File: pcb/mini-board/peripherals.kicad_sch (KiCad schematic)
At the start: 20 parts, among them J2 Conn_02x14_Odd_Even, J3 SD Card Board, J8 SERIAL, U15 SST39SF040, U16 AS6C4008-55, U19 W65C22NxP, U21 W65C51NxP, U22 MAX232, Y1 1.8432 MHz

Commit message: Pre-fourlayerboard commit
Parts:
- J2: value Conn_02x14_Odd_Even -> EXPANSION BUS; footprint Connector_PinHeader_2.54mm:PinHeader_2x14_P2.54mm_Vertical -> Connector_PinHeader_2.54mm:PinHeader_2x20_P2.54mm_Vertical; symbol Connector_Generic:Conn_02x14_Odd_Even -> Connector_Generic:Conn_02x20_Odd_Even
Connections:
- net CA1: now also J2.24 (Pin_24); no longer J2.20 (Pin_20)
- net CA2: now also J2.26 (Pin_26); no longer J2.22 (Pin_22)
- net CB1: now also J2.23 (Pin_23); no longer J2.19 (Pin_19)
- net CB2: now also J2.25 (Pin_25); no longer J2.21 (Pin_21)
- net CLK: now also J2.30 (Pin_30); no longer J2.26 (Pin_26)
- net GND: now also J2.11 (Pin_11), J2.12 (Pin_12), J2.21 (Pin_21), J2.22 (Pin_22), J2.31 (Pin_31), J2.32 (Pin_32), J2.39 (Pin_39), J2.40 (Pin_40); no longer J2.27 (Pin_27), J2.28 (Pin_28)
- net PA4: now also J2.14 (Pin_14); no longer J2.12 (Pin_12)
- net PA5: now also J2.16 (Pin_16); no longer J2.14 (Pin_14)
- net PA6: now also J2.18 (Pin_18); no longer J2.16 (Pin_16)
- net PA7: now also J2.20 (Pin_20); no longer J2.18 (Pin_18)
- net PB4: now also J2.13 (Pin_13); no longer J2.11 (Pin_11)
- net PB5: now also J2.15 (Pin_15); no longer J2.13 (Pin_13)
- net PB6: now also J2.17 (Pin_17); no longer J2.15 (Pin_15)
- net PB7: now also J2.19 (Pin_19); no longer J2.17 (Pin_17)
- net RxD1: now also J2.36 (Pin_36)
- net R/~{W}: now also J2.27 (Pin_27); no longer J2.23 (Pin_23)
- net TxD1: now also J2.34 (Pin_34)
- net VCC: now also J2.37 (Pin_37), J2.38 (Pin_38)
- net ~{NMI}: now also J2.29 (Pin_29); no longer J2.25 (Pin_25)
- net ~{RES}: now also J2.28 (Pin_28); no longer J2.24 (Pin_24)
- net ~{VIA_CS}: now also J2.33 (Pin_33)
- net ~{IRQ} renamed ~{IRQ22}
- net ~{IRQ22}: now also J2.35 (Pin_35); no longer U21.26 (~{IRQ})
- new net ~{IRQ51}: U21.26 (~{IRQ})
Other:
- moved on the sheet: C24

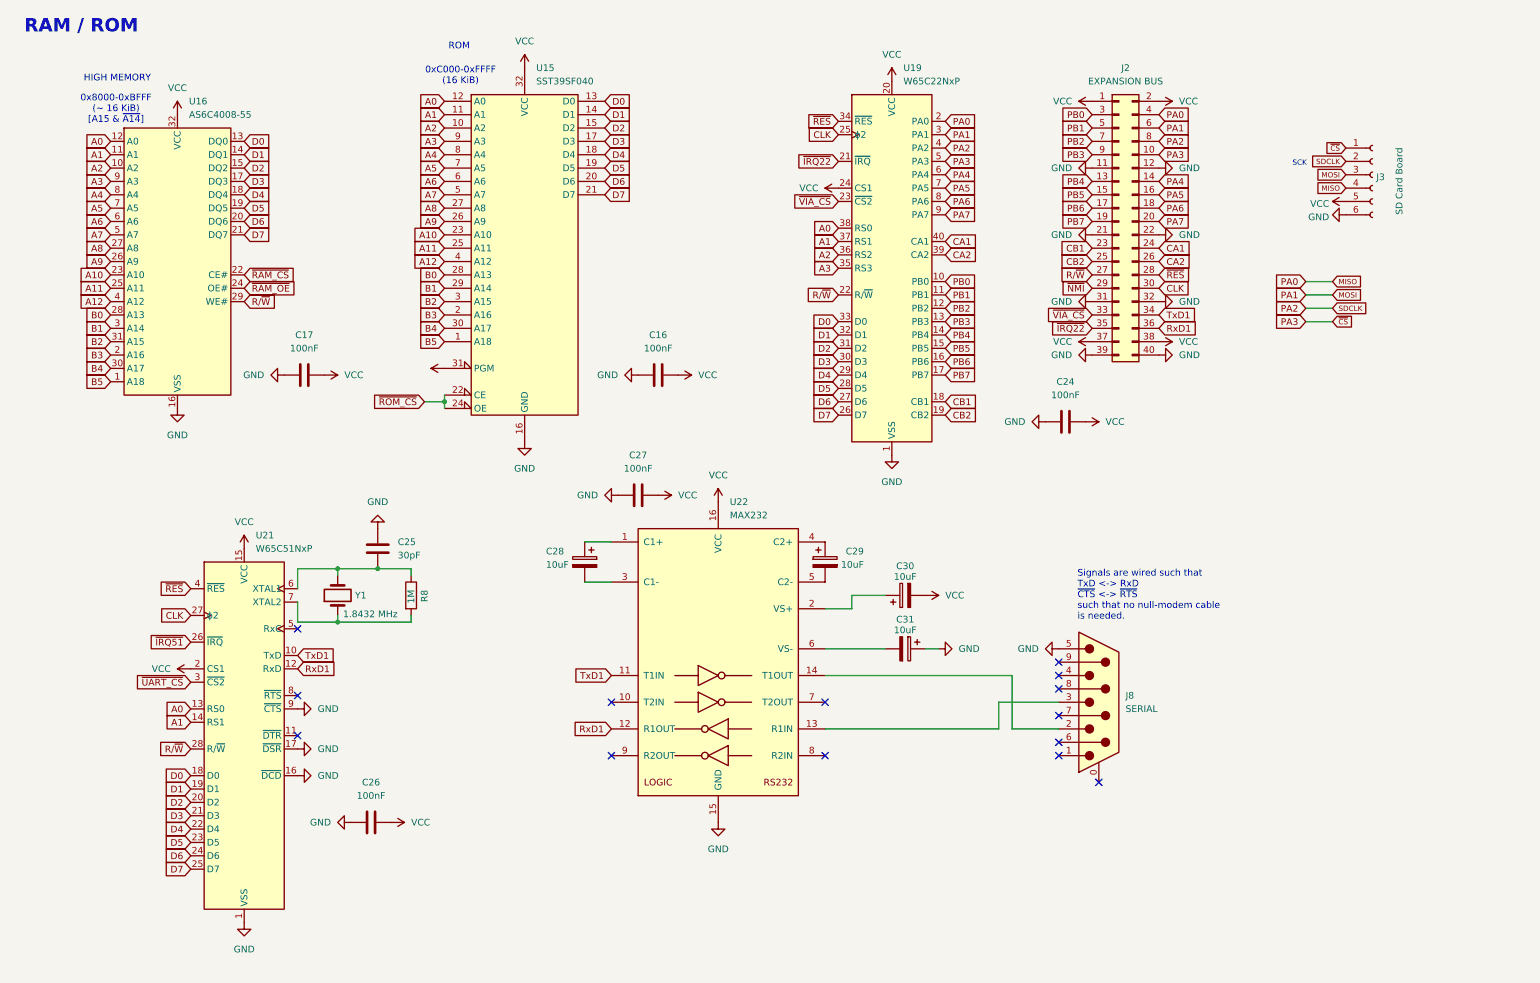
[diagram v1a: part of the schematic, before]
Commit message: Adding documentation to schematics
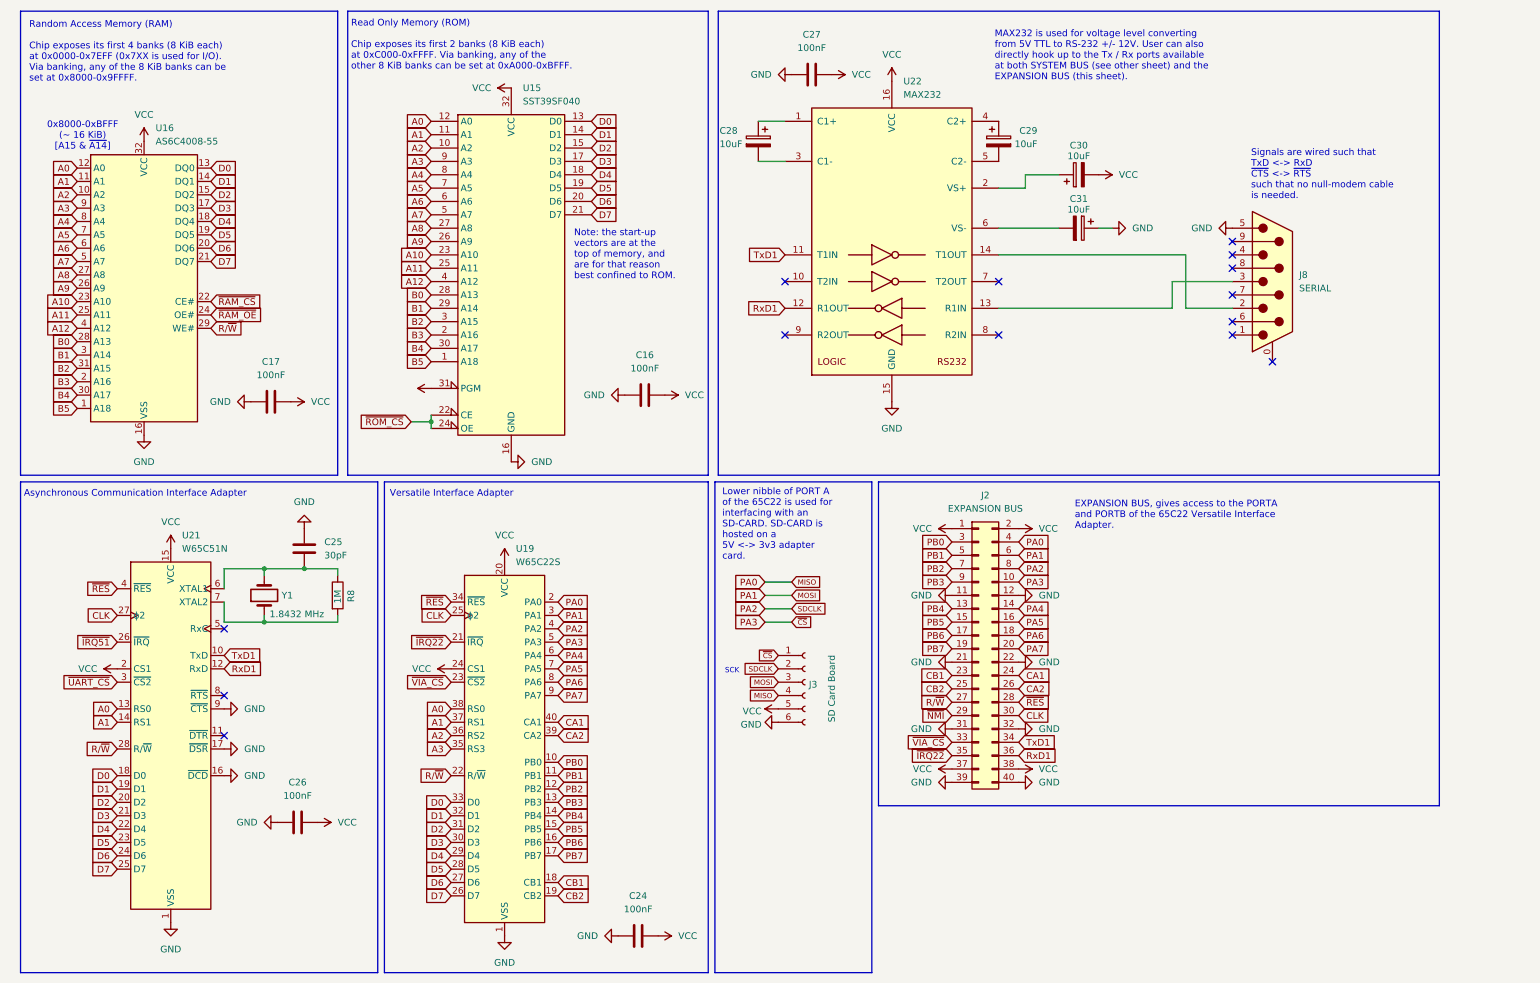
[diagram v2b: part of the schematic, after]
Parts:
- U19: value W65C22NxP -> W65C22S
- U21: value W65C51NxP -> W65C51N
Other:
- note added: "Asynchronous Communication Interface Adapter"
- note added: "EXPANSION BUS, gives access to the PORTA and PORTB of the 65C22 Versatile Interface Adapter."
- note added: "Lower nibble of PORT A of the 65C22 is used for interfacing with an SD-CARD. SD-CARD is hosted on a 5V <-> 3v3 adapter card."
- note added: "MAX232 is used for voltage level converting from 5V TTL to RS-232 +/- 12V. User can also directly hook up to the Tx / Rx ports available at both SYSTEM BUS (see other sheet) and the EXPANSION BUS (this sheet)."
- note added: "Note: the start-up vectors are at the top of memory, and are for that reason best confined to ROM."
- note added: "Random Access Memory (RAM) Chip exposes its first 4 banks (8 KiB each) at 0x0000-0x7EFF (0x7XX is used for I/O). Via banking, any of the 8 KiB banks can be set at 0x8000-0x9FFFF."
- note added: "Read Only Memory (ROM) Chip exposes its first 2 banks (8 KiB each) at 0xC000-0xFFFF. Via banking, any of the other 8 KiB banks can be set at 0xA000-0xBFFF."
- note added: "Versatile Interface Adapter"
- note removed: "0xC000-0xFFFF (16 KiB)"
- note removed: "HIGH MEMORY"
- note removed: "RAM / ROM"
- note removed: "ROM"
- moved on the sheet: C16, C17, C24, C25, C26, C27, C28, C29, C30, C31, J2, J3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

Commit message: Exporting pages
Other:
- title: ByteCradle 6502 - RAM/ROM -> ByteCradle 6502 MINI BOARD
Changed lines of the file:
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@@
 	(paper "A4")
 	(title_block
-		(title "ByteCradle 6502 - RAM/ROM")
-		(date "2025-01-25")
+		(title "ByteCradle 6502 MINI BOARD")
+		(date "2025-05-03")
 		(rev "1")
 	)

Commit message: Adding 10k resistor to IRQ51
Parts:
- added R13: 10k, Resistor_THT:R_Axial_DIN0207_L6.3mm_D2.5mm_P7.62mm_Horizontal, symbol Device:R
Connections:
- net VCC: now also R13.1
- net ~{IRQ51}: now also R13.2
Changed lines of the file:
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@@
 		(color 0 0 0 0)
 	)
+	(junction
+		(at 25.4 133.35)
+		(diameter 0)
+		(color 0 0 0 0)
+	)
 	(no_connect
 		(at 52.07 130.81)
@@
 	(wire
 		(pts
+			(xy 25.4 130.81) (xy 25.4 133.35)
+		)
+		(stroke
+			(width 0)
+			(type default)
+		)
+	)
+	(wire
+		(pts
 			(xy 199.39 69.85) (xy 232.41 69.85)
 		)
@@
 	(wire
 		(pts
+			(xy 22.86 129.54) (xy 22.86 130.81)
+		)
+		(stroke
+			(width 0)
+			(type default)
+		)
+	)
+	(wire
+		(pts
 			(xy 59.69 119.38) (xy 59.69 120.65)
 		)
@@
 	(wire
 		(pts
+			(xy 22.86 133.35) (xy 25.4 133.35)
+		)
+		(stroke
+			(width 0)
+			(type default)
+		)
+	)
+	(wire
+		(pts
 			(xy 154.94 129.54) (xy 160.02 129.54)
 		)
@@
 		)
 	)
+	(wire
+		(pts
+			(xy 25.4 133.35) (xy 31.75 133.35)
+		)
+		(stroke
+			(width 0)
+			(type default)
+		)
+	)
 	(polyline
 		(pts
@@
 		)
 	)
+	(wire
+		(pts
+			(xy 22.86 130.81) (xy 25.4 130.81)
+		)
+		(stroke
+			(width 0)
+			(type default)
+		)
+	)
 	(global_label "~{RAM_OE}"
 		(shape input)
@@
 	(global_label "~{IRQ51}"
 		(shape input)
-		(at 31.75 133.35 180)
+		(at 22.86 133.35 180)
 		(fields_autoplaced yes)
 		(effects
@@
 		)
 		(property "Intersheetrefs" "${INTERSHEET_REFS}"
-			(at 23.1405 133.35 0)
+			(at 14.2505 133.35 0)
 			(effects
 				(font
@@
 	)
 	(symbol
+		(lib_id "Device:R")
+		(at 22.86 125.73 0)
+		(mirror y)
+		(unit 1)
+		(exclude_from_sim no)
+		(in_bom yes)
+		(on_board yes)
+		(dnp no)
+		(property "Reference" "R13"
+			(at 20.574 125.73 90)
+			(effects
+				(font
+					(size 1.27 1.27)
+				)
+			)
+		)
+		(property "Value" "10k"
+			(at 22.86 125.73 90)
+			(effects
+				(font
+					(size 1.27 1.27)
+				)
+			)
+		)
+		(property "Footprint" "Resistor_THT:R_Axial_DIN0207_L6.3mm_D2.5mm_P7.62mm_Horizontal"
+			(at 24.638 125.73 90)
+			(effects
+				(font
+					(size 1.27 1.27)
+				)
+				(hide yes)
+			)
+		)
+		(property "Datasheet" "~"
+			(at 22.86 125.73 0)
+			(effects
+				(font
+					(size 1.27 1.27)
+				)
+				(hide yes)
+			)
+		)
+		(property "Description" "Resistor"
+			(at 22.86 125.73 0)
+			(effects
+				(font
+					(size 1.27 1.27)
+				)
+				(hide yes)
+			)
+		)
+		(pin "2"
+		)
+		(pin "1"
+		)
+		(instances
+			(project "mini-board"
+				(path "/70c9e9e4-d560-4927-af97-189b3a969059/5c333674-eefb-4707-94ed-6c6ed8cb8074"
+					(reference "R13")
+					(unit 1)
+				)
+			)
+		)
+	)
+	(symbol
 		(lib_id "power:GND")
 		(at 36.83 93.98 0)
@@
 					(unit 1)
 				)
+			)
+		)
+	)
+	(symbol
+		(lib_id "power:VCC")
+		(at 22.86 121.92 0)
+		(unit 1)
+		(exclude_from_sim no)
+		(in_bom yes)
+		(on_board yes)
+		(dnp no)
+		(fields_autoplaced yes)
+		(property "Reference" "#PWR030"
+			(at 22.86 125.73 0)
+			(effects
+				(font
+					(size 1.27 1.27)
+				)
+				(hide yes)
+			)
+		)
+		(property "Value" "VCC"
+			(at 22.8599 118.11 90)
+			(effects
+				(font
+					(size 1.27 1.27)
+				)
+				(justify left)
+			)
+		)
+		(property "Footprint" ""
+			(at 22.86 121.92 0)
+			(effects
+				(font
+					(size 1.27 1.27)
+				)
+				(hide yes)
+			)
+		)
+		(property "Datasheet" ""
+			(at 22.86 121.92 0)
+			(effects
+				(font
+					(size 1.27 1.27)
+				)
+				(hide yes)
+			)
+		)
+		(property "Description" "Power symbol creates a global label with name \"VCC\""
+			(at 22.86 121.92 0)
+			(effects
+				(font
+					(size 1.27 1.27)
+				)
+				(hide yes)
+			)
+		)
+		(pin "1"
+		)
+		(instances
+			(project "mini-board"
+				(path "/70c9e9e4-d560-4927-af97-189b3a969059/5c333674-eefb-4707-94ed-6c6ed8cb8074"
+					(reference "#PWR030")
+					(unit 1)
+				)
